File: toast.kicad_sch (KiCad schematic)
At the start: 0 parts

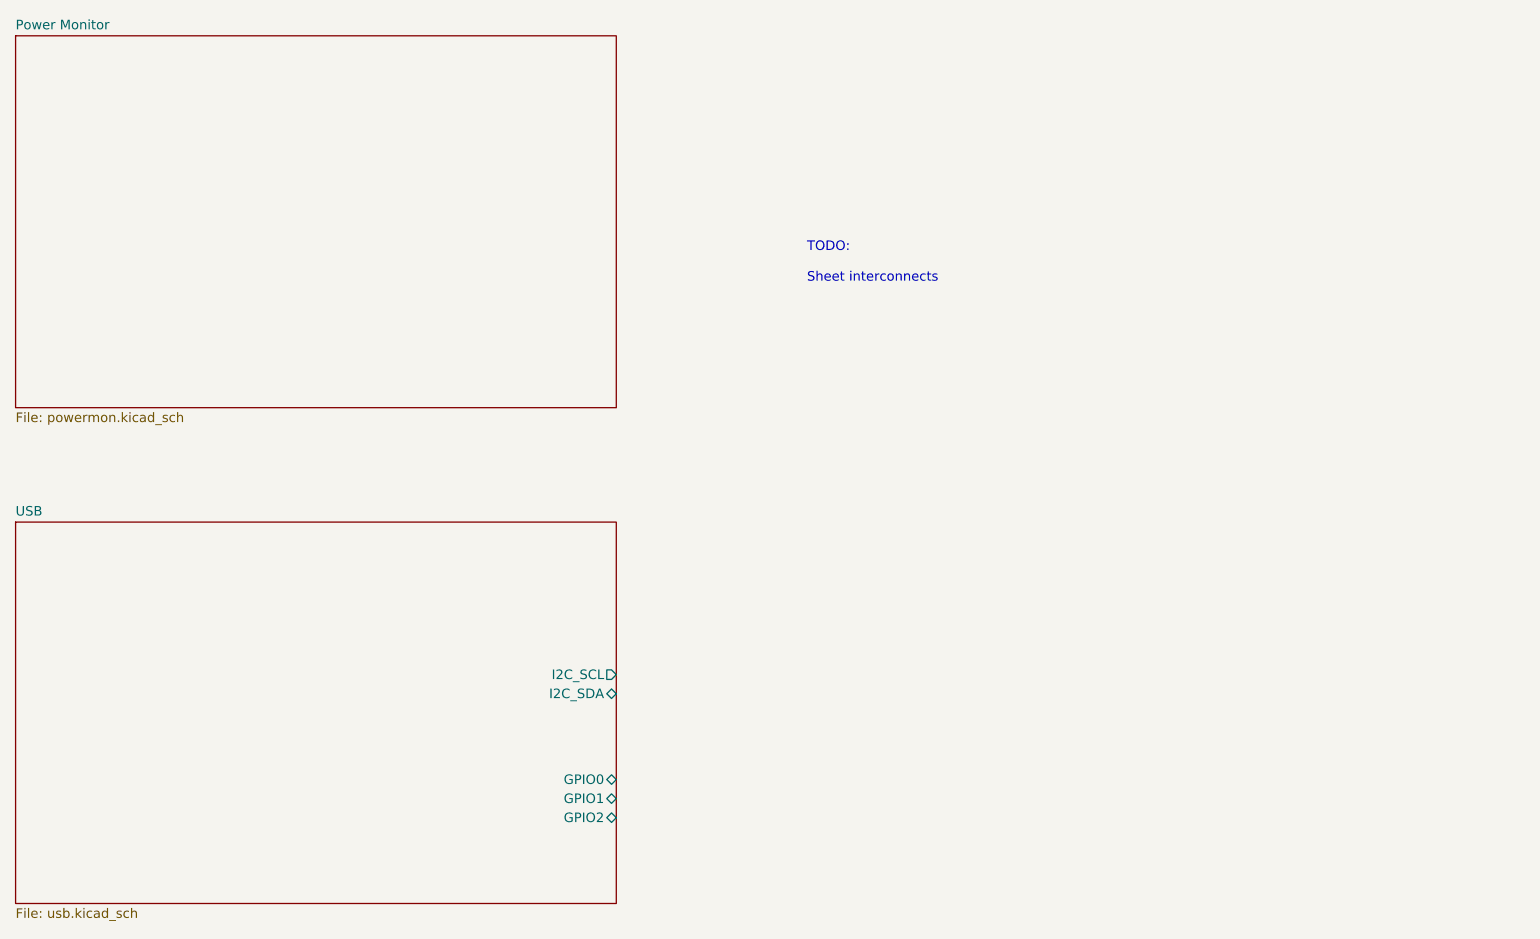
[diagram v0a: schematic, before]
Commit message: WiP: PAC1953 power monitor
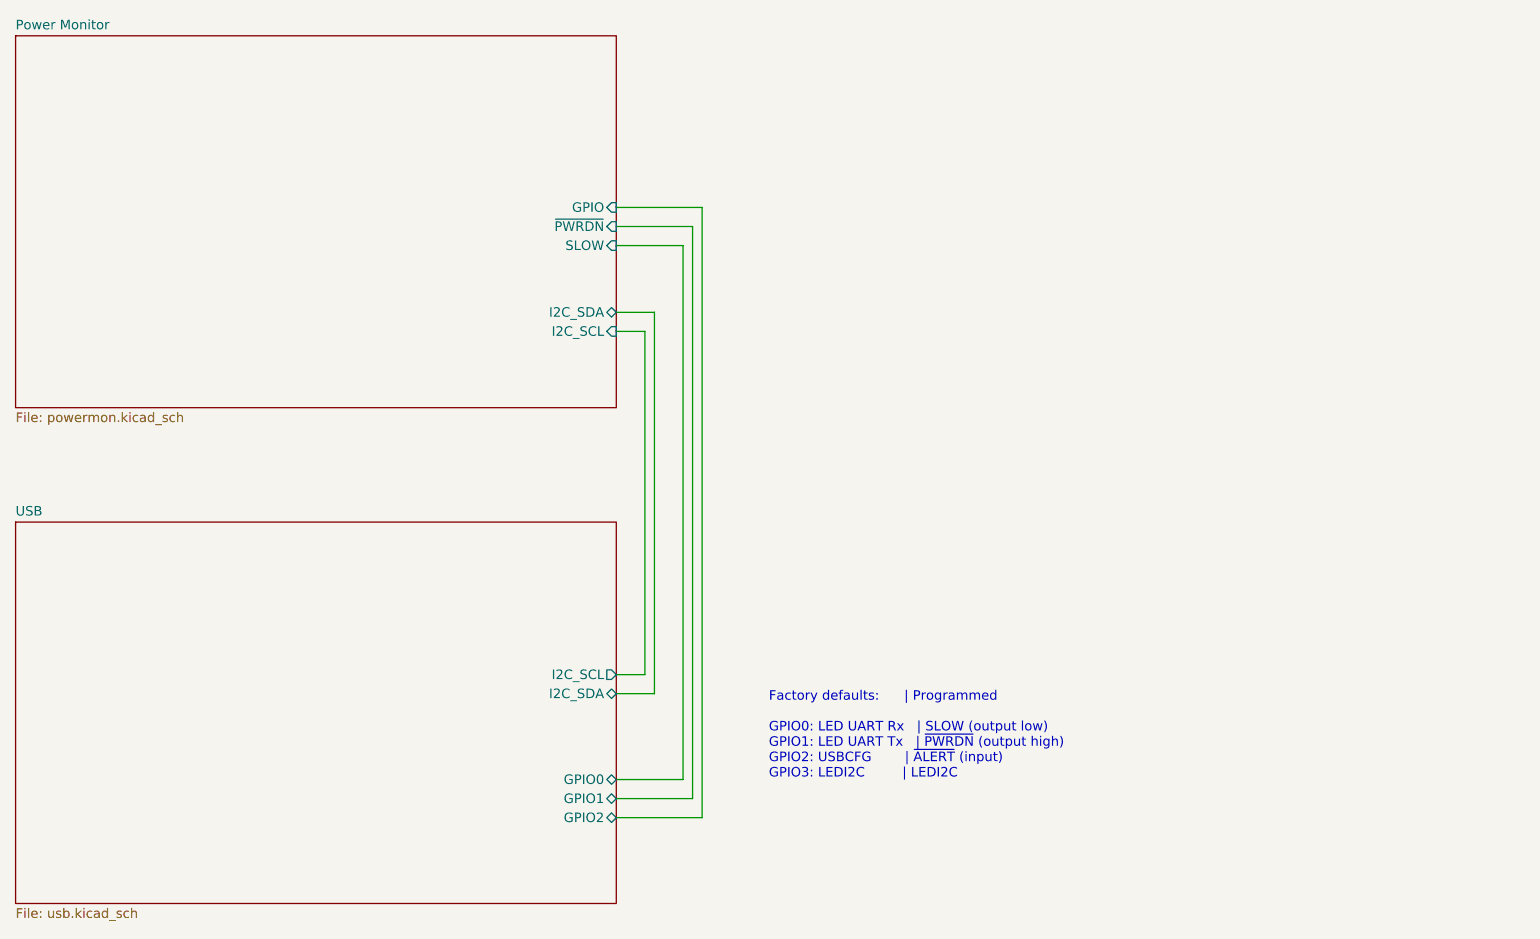
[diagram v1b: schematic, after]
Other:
- sheet Power Monitor ports: added GPIO, I2C_SCL, I2C_SDA, SLOW, ~{PWRDN}; removed none
- note added: "Factory defaults: | Programmed GPIO0: LED UART Rx | SLOW (output low) GPIO1: LED UART Tx | ~{PWRDN} (output high) GPIO2: USBCFG | ~{ALERT} (input) GPIO3: LEDI2C | LEDI2C"
- note removed: "TODO: Sheet interconnects"
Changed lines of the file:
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@@
 (kicad_sch (version 20211123) (generator eeschema)
   (paper "A4")
-  (text "TODO:\n\nSheet interconnects" (at 139.7 62.23 0)
+  (wire (pts (xy 114.3 54.61) (xy 124.46 54.61))
+    (stroke (width 0) (type default) (color 0 0 0 0))
+  )
+  (wire (pts (xy 118.11 68.58) (xy 118.11 114.3))
+    (stroke (width 0) (type default) (color 0 0 0 0))
+  )
+  (wire (pts (xy 124.46 54.61) (xy 124.46 130.81))
+    (stroke (width 0) (type default) (color 0 0 0 0))
+  )
+  (wire (pts (xy 114.3 68.58) (xy 118.11 68.58))
+    (stroke (width 0) (type default) (color 0 0 0 0))
+  )
+  (wire (pts (xy 124.46 130.81) (xy 114.3 130.81))
+    (stroke (width 0) (type default) (color 0 0 0 0))
+  )
+  (wire (pts (xy 125.73 133.35) (xy 114.3 133.35))
+    (stroke (width 0) (type default) (color 0 0 0 0))
+  )
+  (wire (pts (xy 118.11 114.3) (xy 114.3 114.3))
+    (stroke (width 0) (type default) (color 0 0 0 0))
+  )
+  (wire (pts (xy 114.3 57.15) (xy 123.19 57.15))
+    (stroke (width 0) (type default) (color 0 0 0 0))
+  )
+  (wire (pts (xy 123.19 128.27) (xy 114.3 128.27))
+    (stroke (width 0) (type default) (color 0 0 0 0))
+  )
+  (wire (pts (xy 114.3 52.07) (xy 125.73 52.07))
+    (stroke (width 0) (type default) (color 0 0 0 0))
+  )
+  (wire (pts (xy 119.38 116.84) (xy 114.3 116.84))
+    (stroke (width 0) (type default) (color 0 0 0 0))
+  )
+  (wire (pts (xy 119.38 66.04) (xy 119.38 116.84))
+    (stroke (width 0) (type default) (color 0 0 0 0))
+  )
+  (wire (pts (xy 125.73 52.07) (xy 125.73 133.35))
+    (stroke (width 0) (type default) (color 0 0 0 0))
+  )
+  (wire (pts (xy 114.3 66.04) (xy 119.38 66.04))
+    (stroke (width 0) (type default) (color 0 0 0 0))
+  )
+  (wire (pts (xy 123.19 57.15) (xy 123.19 128.27))
+    (stroke (width 0) (type default) (color 0 0 0 0))
+  )
+  (text "Factory defaults:      | Programmed\n\nGPIO0: LED UART Rx   | SLOW (output low)\nGPIO1: LED UART Tx   | ~{PWRDN} (output high)\nGPIO2: USBCFG        | ~{ALERT} (input)\nGPIO3: LEDI2C         | LEDI2C"
+    (at 134.62 128.27 0)
     (effects (font (size 1.27 1.27)) (justify left bottom))
   )
@@
       (effects (font (size 1.27 1.27)) (justify left top))
     )
+    (pin "I2C_SCL" input (at 114.3 68.58 0)
+      (effects (font (size 1.27 1.27)) (justify right))
+    )
+    (pin "I2C_SDA" bidirectional (at 114.3 66.04 0)
+      (effects (font (size 1.27 1.27)) (justify right))
+    )
+    (pin "SLOW" input (at 114.3 57.15 0)
+      (effects (font (size 1.27 1.27)) (justify right))
+    )
+    (pin "~{PWRDN}" input (at 114.3 54.61 0)
+      (effects (font (size 1.27 1.27)) (justify right))
+    )
+    (pin "GPIO" input (at 114.3 52.07 0)
+      (effects (font (size 1.27 1.27)) (justify right))
+    )
   )
   (sheet (at 34.29 93.98) (size 80.01 50.8) (fields_autoplaced)
@@
       (reference "#PWR?") (unit 1) (value "GND") (footprint "")
     )
+    (path "/509457db-eedd-4ad9-89dd-afa4c46733b6/1a613bc6-1d83-49de-a5d1-cb6ecebc8fdf"
+      (reference "#PWR?") (unit 1) (value "+3V3") (footprint "")
+    )
     (path "/85a187b5-2adf-4f49-9f19-442d04950f80/1aee80e0-d5ab-4041-a69f-25c9526af2c9"
       (reference "#PWR?") (unit 1) (value "+5V") (footprint "")
     )
+    (path "/509457db-eedd-4ad9-89dd-afa4c46733b6/28ecf7f2-034a-4e0b-a3f6-1c81b9438c81"
+      (reference "#PWR?") (unit 1) (value "GND") (footprint "")
+    )
     (path "/509457db-eedd-4ad9-89dd-afa4c46733b6/2dc3edb5-1e52-4f89-b49a-bc9320992824"
       (reference "#PWR?") (unit 1) (value "+3V3") (footprint "")
@@
     )
     (path "/85a187b5-2adf-4f49-9f19-442d04950f80/37047cfa-bb34-4160-bb59-973a84aec4b6"
+      (reference "#PWR?") (unit 1) (value "+3V3") (footprint "")
+    )
+    (path "/509457db-eedd-4ad9-89dd-afa4c46733b6/39a8cd39-294a-4c8a-99d7-71b35feea45f"
+      (reference "#PWR?") (unit 1) (value "+3V3") (footprint "")
+    )
+    (path "/509457db-eedd-4ad9-89dd-afa4c46733b6/4004288d-bf7f-41fb-ab8f-dbd688fa294e"
       (reference "#PWR?") (unit 1) (value "+3V3") (footprint "")
     )
@@
       (reference "#PWR?") (unit 1) (value "+5V") (footprint "")
     )
+    (path "/509457db-eedd-4ad9-89dd-afa4c46733b6/cb1b217a-7e7a-4fe5-8f21-8a2122dee06d"
+      (reference "#PWR?") (unit 1) (value "GND") (footprint "")
+    )
     (path "/85a187b5-2adf-4f49-9f19-442d04950f80/f4e5e69b-1de1-4d60-b70c-9d544d629f28"
       (reference "#PWR?") (unit 1) (value "GND") (footprint "")
@@
     (path "/85a187b5-2adf-4f49-9f19-442d04950f80/f8f8ba8e-6553-420b-a9fa-edfa007ab153"
       (reference "#PWR?") (unit 1) (value "GND") (footprint "")
+    )
+    (path "/509457db-eedd-4ad9-89dd-afa4c46733b6/1fa55ac0-fd30-4a39-99b2-2303d9b92e3d"
+      (reference "C?") (unit 1) (value "1uF") (footprint "")
     )
     (path "/85a187b5-2adf-4f49-9f19-442d04950f80/60057a8e-6c12-43d5-81a0-4acd8f8fc5bb"
       (reference "C?") (unit 1) (value "1uF") (footprint "")
     )
+    (path "/509457db-eedd-4ad9-89dd-afa4c46733b6/71596cf3-8544-4b7a-8c91-d72ec1d11c78"
+      (reference "C?") (unit 1) (value "0.1uF") (footprint "")
+    )
     (path "/85a187b5-2adf-4f49-9f19-442d04950f80/72befada-e2cc-4bfd-829b-0ba404fd7d8f"
       (reference "C?") (unit 1) (value "0.1uF") (footprint "")
@@
     )
     (path "/509457db-eedd-4ad9-89dd-afa4c46733b6/095d800e-c57c-4002-b939-11f909c8c461"
-      (reference "R?") (unit 1) (value "5.1k") (footprint "")
+      (reference "R?") (unit 1) (value "10k") (footprint "")
     )
     (path "/509457db-eedd-4ad9-89dd-afa4c46733b6/0a2ffd6c-a897-42e4-8c34-7d6acdbe07a5"
-      (reference "R?") (unit 1) (value "5.1k") (footprint "")
+      (reference "R?") (unit 1) (value "10k") (footprint "")
     )
     (path "/85a187b5-2adf-4f49-9f19-442d04950f80/943b5829-0132-4108-bdb5-1613d62772bb"
@@
       (reference "R?") (unit 1) (value "5.1k") (footprint "")
     )
+    (path "/509457db-eedd-4ad9-89dd-afa4c46733b6/d65d2559-1570-4c94-b5d4-607e42eab7c8"
+      (reference "R?") (unit 1) (value "10k") (footprint "")
+    )
     (path "/85a187b5-2adf-4f49-9f19-442d04950f80/e0bb5824-4a41-4bb9-b622-0a67bd30c4c3"

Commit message: PAC1953 shunt resistors, terminals
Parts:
- added H? (x3): MountingHole_Pad, symbol Mechanical:MountingHole_Pad
- added H?: (no value), symbol Mechanical:MountingHole_Pad
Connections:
- new net GND: H?.1, H?.1, H?.1, H?.1

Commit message: ERC
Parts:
- gave numbers to parts that had none: 4

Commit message: Associate built-in footprints
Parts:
- H1: value (none) -> MountingHole_Pad; footprint (none) -> MountingHole:MountingHole_2.2mm_M2_Pad
- H2, H3, H4: footprint (none) -> MountingHole:MountingHole_2.2mm_M2_Pad

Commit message: Add stencil alignment holes
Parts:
- added H5, H6, H7, H8: StencilAlignmentHole, symbol Mechanical:MountingHole
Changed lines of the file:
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@@
     (pin "1")
+  )
+  (symbol (lib_id "Mechanical:MountingHole") (at 200.66 102.87 0) (unit 1)
+    (in_bom yes) (on_board yes) (fields_autoplaced)
+    (property "Reference" "H6" (id 0) (at 203.2 101.5999 0)
+      (effects (font (size 1.27 1.27)) (justify left))
+    )
+    (property "Value" "StencilAlignmentHole" (id 1) (at 203.2 104.1399 0)
+      (effects (font (size 1.27 1.27)) (justify left))
+    )
+    (property "Footprint" "" (id 2) (at 200.66 102.87 0)
+      (effects (font (size 1.27 1.27)) hide)
+    )
+    (property "Datasheet" "~" (id 3) (at 200.66 102.87 0)
+      (effects (font (size 1.27 1.27)) hide)
+    )
+  )
+  (symbol (lib_id "Mechanical:MountingHole") (at 200.66 96.52 0) (unit 1)
+    (in_bom yes) (on_board yes) (fields_autoplaced)
+    (property "Reference" "H5" (id 0) (at 203.2 95.2499 0)
+      (effects (font (size 1.27 1.27)) (justify left))
+    )
+    (property "Value" "StencilAlignmentHole" (id 1) (at 203.2 97.7899 0)
+      (effects (font (size 1.27 1.27)) (justify left))
+    )
+    (property "Footprint" "" (id 2) (at 200.66 96.52 0)
+      (effects (font (size 1.27 1.27)) hide)
+    )
+    (property "Datasheet" "~" (id 3) (at 200.66 96.52 0)
+      (effects (font (size 1.27 1.27)) hide)
+    )
   )
   (symbol (lib_id "Mechanical:MountingHole_Pad") (at 212.09 45.72 0) (unit 1)
@@
     (pin "1")
   )
+  (symbol (lib_id "Mechanical:MountingHole") (at 200.66 109.22 0) (unit 1)
+    (in_bom yes) (on_board yes) (fields_autoplaced)
+    (property "Reference" "H7" (id 0) (at 203.2 107.9499 0)
+      (effects (font (size 1.27 1.27)) (justify left))
+    )
+    (property "Value" "StencilAlignmentHole" (id 1) (at 203.2 110.4899 0)
+      (effects (font (size 1.27 1.27)) (justify left))
+    )
+    (property "Footprint" "" (id 2) (at 200.66 109.22 0)
+      (effects (font (size 1.27 1.27)) hide)
+    )
+    (property "Datasheet" "~" (id 3) (at 200.66 109.22 0)
+      (effects (font (size 1.27 1.27)) hide)
+    )
+  )
   (symbol (lib_id "Mechanical:MountingHole_Pad") (at 189.23 64.77 0) (unit 1)
     (in_bom yes) (on_board yes) (fields_autoplaced)
@@
     )
     (pin "1")
+  )
+  (symbol (lib_id "Mechanical:MountingHole") (at 200.66 115.57 0) (unit 1)
+    (in_bom yes) (on_board yes) (fields_autoplaced)
+    (property "Reference" "H8" (id 0) (at 203.2 114.2999 0)
+      (effects (font (size 1.27 1.27)) (justify left))
+    )
+    (property "Value" "StencilAlignmentHole" (id 1) (at 203.2 116.8399 0)
+      (effects (font (size 1.27 1.27)) (justify left))
+    )
+    (property "Footprint" "" (id 2) (at 200.66 115.57 0)
+      (effects (font (size 1.27 1.27)) hide)
+    )
+    (property "Datasheet" "~" (id 3) (at 200.66 115.57 0)
+      (effects (font (size 1.27 1.27)) hide)
+    )
   )
   (symbol (lib_id "Mechanical:MountingHole_Pad") (at 189.23 45.72 0) (unit 1)
@@
       (reference "H4") (unit 1) (value "MountingHole_Pad") (footprint "MountingHole:MountingHole_2.2mm_M2_Pad")
     )
+    (path "/4ab193e8-4247-4612-8b8f-92512a1194ff"
+      (reference "H5") (unit 1) (value "StencilAlignmentHole") (footprint "")
+    )
+    (path "/3d41835d-e1d0-42e4-a87b-c05bec5fd2a8"
+      (reference "H6") (unit 1) (value "StencilAlignmentHole") (footprint "")
+    )
+    (path "/a357c15a-be34-4c0d-b809-4d48ecbd3390"
+      (reference "H7") (unit 1) (value "StencilAlignmentHole") (footprint "")
+    )
+    (path "/dc0f4484-4ebf-4f4b-ae84-9e432f53ece0"
+      (reference "H8") (unit 1) (value "StencilAlignmentHole") (footprint "")
+    )
     (path "/509457db-eedd-4ad9-89dd-afa4c46733b6/cccc183d-f591-443c-b10b-559e23d1baf1"
